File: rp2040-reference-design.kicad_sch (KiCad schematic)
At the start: 35 parts, among them J2 Conn_01x10_Pin, J3 Conn_01x10_Pin, U1 RP2040, U2 W25Q128JVS, Y1 12mhz ABM8-272-T

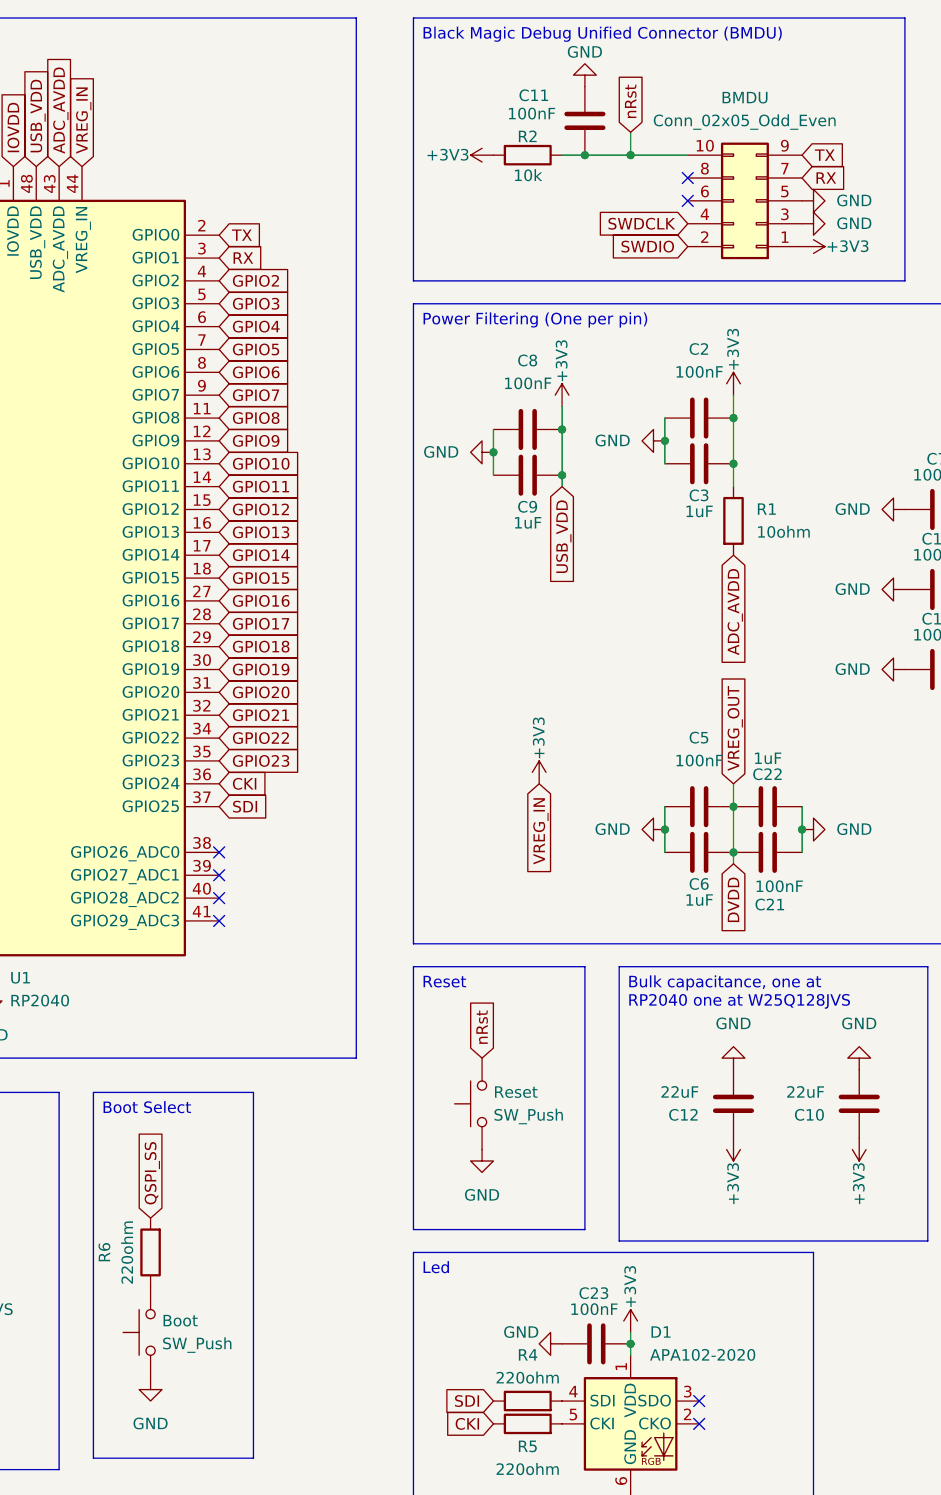
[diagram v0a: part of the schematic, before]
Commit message: fix: mcorrected crystal pinout
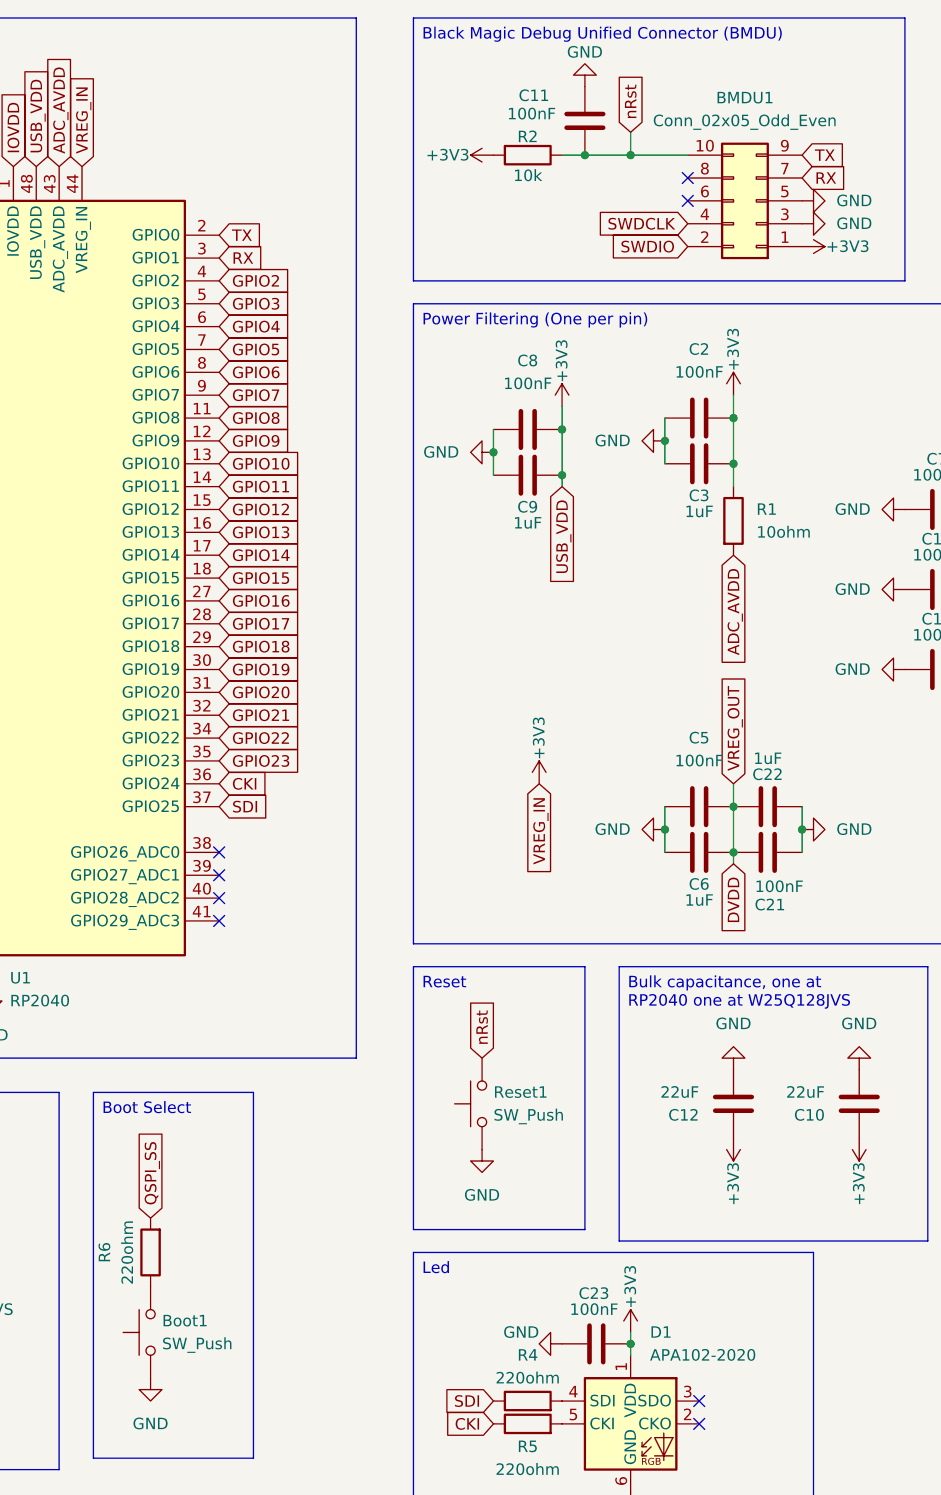
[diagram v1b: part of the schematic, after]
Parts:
- Y1: footprint Crystal:Crystal_SMD_3225-4Pin_3.2x2.5mm -> Library:ABRACON ABM8-272-T3
- renumbered BMDU to BMDU1, Boot to Boot1, Reset to Reset1
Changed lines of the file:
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@@
 		(dnp no)
 		(fields_autoplaced yes)
-		(property "Reference" "Reset"
+		(property "Reference" "Reset1"
 			(at 124.46 138.4299 90)
 			(effects
@@
 			(project ""
 				(path "/d9eb9251-8b4f-4594-87db-d1b592086b55"
-					(reference "Reset")
+					(reference "Reset1")
 					(unit 1)
 				)
@@
 			)
 		)
-		(property "Footprint" "Crystal:Crystal_SMD_3225-4Pin_3.2x2.5mm"
+		(property "Footprint" "Library:ABRACON ABM8-272-T3"
 			(at 39.37 93.98 0)
 			(effects
@@
 		(dnp no)
 		(fields_autoplaced yes)
-		(property "Reference" "BMDU"
+		(property "Reference" "BMDU1"
 			(at 152.4 27.94 0)
 			(effects
@@
 			(project ""
 				(path "/d9eb9251-8b4f-4594-87db-d1b592086b55"
-					(reference "BMDU")
+					(reference "BMDU1")
 					(unit 1)
 				)
@@
 		(dnp no)
 		(fields_autoplaced yes)
-		(property "Reference" "Boot"
+		(property "Reference" "Boot1"
 			(at 87.63 163.8299 90)
 			(effects
@@
 			(project "rp2040-reference-design"
 				(path "/d9eb9251-8b4f-4594-87db-d1b592086b55"
-					(reference "Boot")
+					(reference "Boot1")
 					(unit 1)
 				)
